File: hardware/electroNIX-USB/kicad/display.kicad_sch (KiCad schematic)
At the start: 69 parts, among them Q10 MMBTA42, Q11 MMBTA92, Q12 MMBTA42, Q13 MMBTA42, Q14 MMBTA42, Q15 MMBTA42, Q16 MMBTA42, Q17 MMBTA42, Q18 MMBTA42, Q19 MMBTA42, Q20 MMBTA42, Q21 MMBTA42, Q22 MMBTA42, Q23 MMBTA42, Q4 MMBTA42, Q5 MMBTA92, Q6 MMBTA42, Q7 MMBTA92, Q8 MMBTA42, Q9 MMBTA92

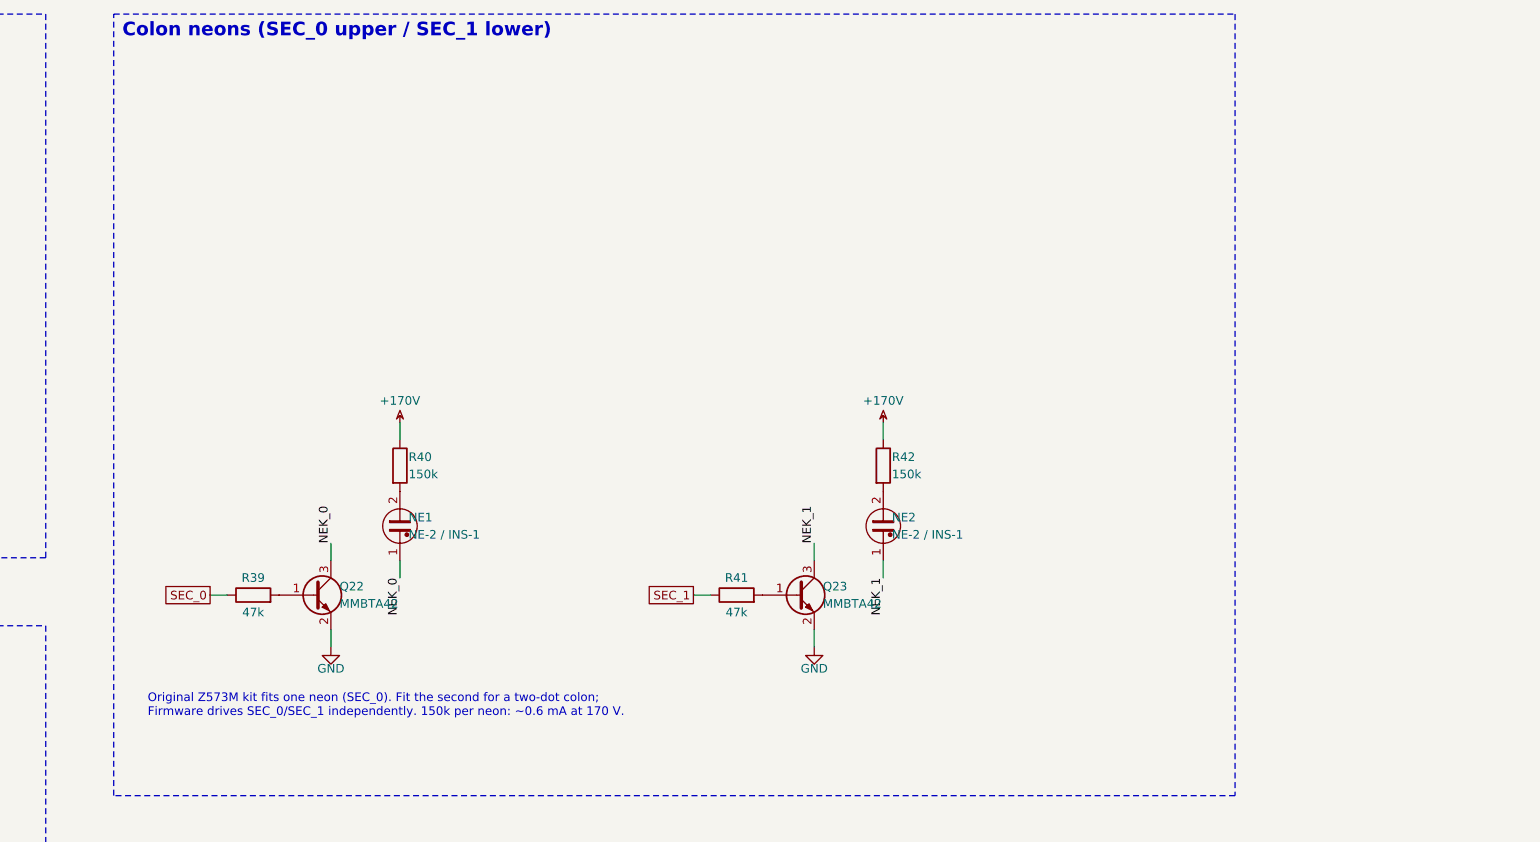
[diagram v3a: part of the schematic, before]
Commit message: electroNIX-USB: socket-adapter footprint, 0.1in neons, 4-tube PCB placement (WIP)
- Z573M socket pins on the electroNIX-2 adapter's 12.6 mm outer ring
  (default footprint), and the direct 9.53 mm footprint resized for the
  1.48 mm socket pins
- Neon_P2.54mm footprint. 6 tubes: HH:MM colon on SEC_0, MM:SS on SEC_1
- SET is a right-angle tact switch; RESET/BOOT use KMR2; low-voltage anode
  resistors moved to 0805
- source/pcb.py: builds the board from the netlist (placement, net
  classes, ESP32 antenna keepout, Freerouting, GND pours, DRC);
  source/fab.sh: fab outputs
- 4-tube board placed (102 x 66 mm, the original kit size), not yet routed

Co-Authored-By: Claude Opus 5.5 <noreply@anthropic.com>
Claude-Session: https://claude.ai/code/session_01AFMfevKEKDGbci8uJGhf4W
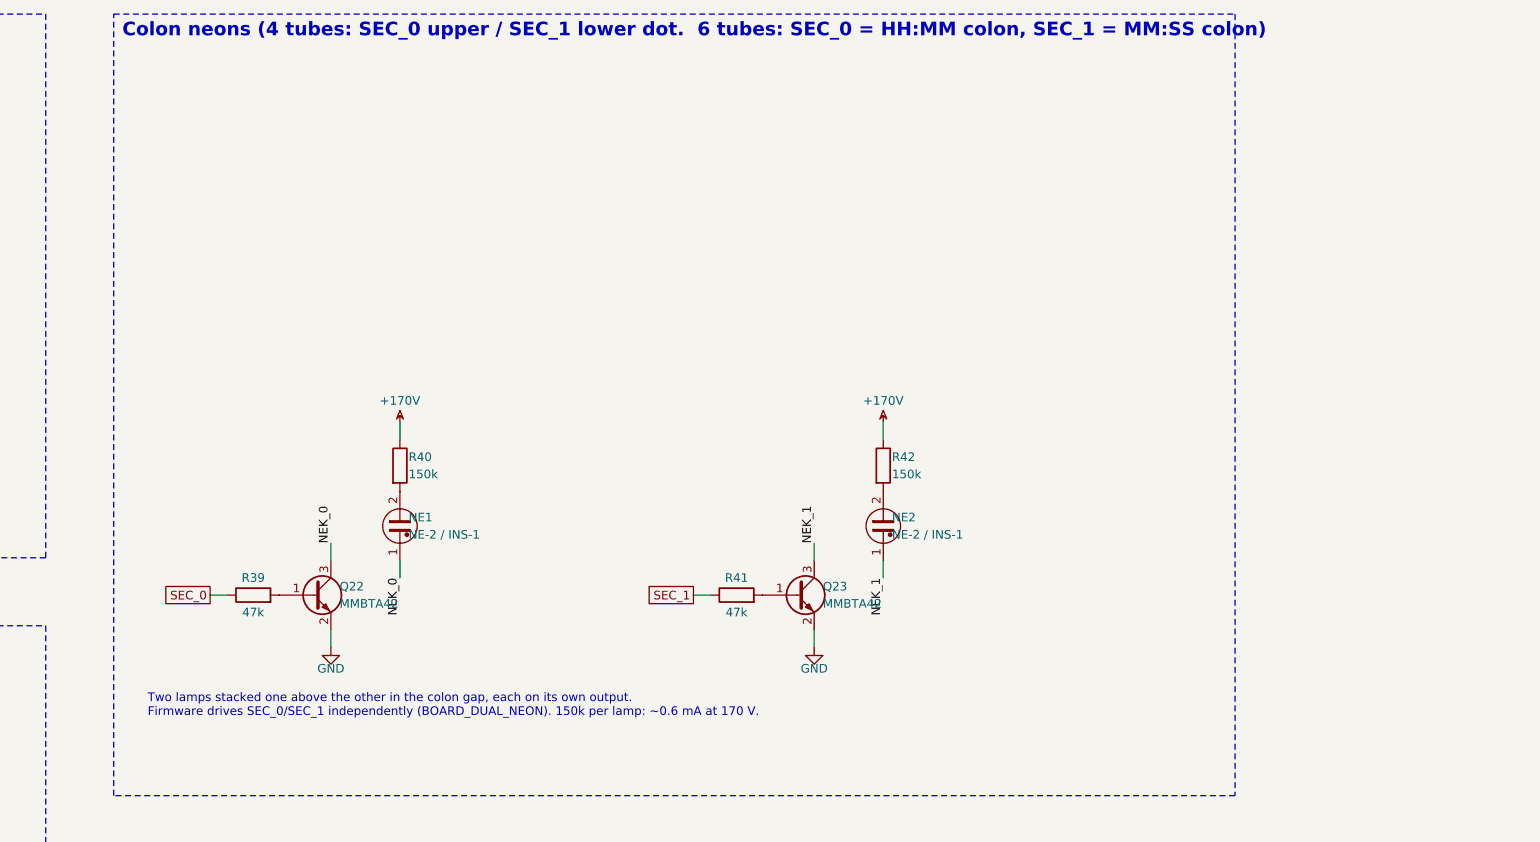
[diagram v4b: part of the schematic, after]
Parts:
- N1, N2, N3, N4: footprint electronix:Nixie_RFT_Z573M -> electronix:Nixie_RFT_Z573M_Adapter
- NE1, NE2: footprint (none) -> electronix:Neon_P2.54mm
- R15, R16, R19, R20, R23, R24, R27, R28: footprint Resistor_SMD:R_1206_3216Metric -> Resistor_SMD:R_0805_2012Metric
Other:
- note added: "Colon neons (4 tubes: SEC_0 upper / SEC_1 lower dot. 6 tubes: SEC_0 = HH:MM colon, SEC_1 = MM:SS colon)"
- note added: "Two lamps stacked one above the other in the colon gap, each on its own output. Firmware drives SEC_0/SEC_1 independently (BOARD_DUAL_NEON). 150k per lamp: ~0.6 mA at 170 V."
- note removed: "Colon neons (SEC_0 upper / SEC_1 lower)"
- note removed: "Original Z573M kit fits one neon (SEC_0). Fit the second for a two-dot colon; Firmware drives SEC_0/SEC_1 independently. 150k per neon: ~0.6 mA at 170 V."
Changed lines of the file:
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@@
       (type none))
 )
-  (text "Colon neons (SEC_0 upper / SEC_1 lower)"
+  (text "Colon neons (4 tubes: SEC_0 upper / SEC_1 lower dot.  6 tubes: SEC_0 = HH:MM colon, SEC_1 = MM:SS colon)"
     (at 411.27 26.27 0)
     (effects
@@
       (justify left top))
 )
-  (text "Original Z573M kit fits one neon (SEC_0). Fit the second for a two-dot colon;\nFirmware drives SEC_0/SEC_1 independently. 150k per neon: ~0.6 mA at 170 V."
+  (text "Two lamps stacked one above the other in the colon gap, each on its own output.\nFirmware drives SEC_0/SEC_1 independently (BOARD_DUAL_NEON). 150k per lamp: ~0.6 mA at 170 V."
     (at 415 125 0)
     (effects
@@
           (size 1.27 1.27))
         (justify left)))
-    (property "Footprint" "Resistor_SMD:R_1206_3216Metric"
+    (property "Footprint" "Resistor_SMD:R_0805_2012Metric"
       (at 52.07 63.5 0)
       (effects
@@
           (size 1.27 1.27))
         (justify left)))
-    (property "Footprint" "Resistor_SMD:R_1206_3216Metric"
+    (property "Footprint" "Resistor_SMD:R_0805_2012Metric"
       (at 59.69 76.2 0)
       (effects
@@
           (size 1.27 1.27))
         (justify left)))
-    (property "Footprint" "Resistor_SMD:R_1206_3216Metric"
+    (property "Footprint" "Resistor_SMD:R_0805_2012Metric"
       (at 142.24 63.5 0)
       (effects
@@
           (size 1.27 1.27))
         (justify left)))
-    (property "Footprint" "Resistor_SMD:R_1206_3216Metric"
+    (property "Footprint" "Resistor_SMD:R_0805_2012Metric"
       (at 149.86 76.2 0)
       (effects
@@
           (size 1.27 1.27))
         (justify left)))
-    (property "Footprint" "Resistor_SMD:R_1206_3216Metric"
+    (property "Footprint" "Resistor_SMD:R_0805_2012Metric"
       (at 232.41 63.5 0)
       (effects
@@
           (size 1.27 1.27))
         (justify left)))
-    (property "Footprint" "Resistor_SMD:R_1206_3216Metric"
+    (property "Footprint" "Resistor_SMD:R_0805_2012Metric"
       (at 240.03 76.2 0)
       (effects
@@
           (size 1.27 1.27))
         (justify left)))
-    (property "Footprint" "Resistor_SMD:R_1206_3216Metric"
+    (property "Footprint" "Resistor_SMD:R_0805_2012Metric"
       (at 322.58 63.5 0)
       (effects
@@
           (size 1.27 1.27))
         (justify left)))
-    (property "Footprint" "Resistor_SMD:R_1206_3216Metric"
+    (property "Footprint" "Resistor_SMD:R_0805_2012Metric"
       (at 330.2 76.2 0)
       (effects
@@
           (size 1.27 1.27))
         (justify left)))
-    (property "Footprint" "electronix:Nixie_RFT_Z573M"
+    (property "Footprint" "electronix:Nixie_RFT_Z573M_Adapter"
       (at 59.69 160.02 0)
       (effects
@@
           (size 1.27 1.27))
         (justify left)))
-    (property "Footprint" "electronix:Nixie_RFT_Z573M"
+    (property "Footprint" "electronix:Nixie_RFT_Z573M_Adapter"
       (at 149.86 160.02 0)
       (effects
@@
           (size 1.27 1.27))
         (justify left)))
-    (property "Footprint" "electronix:Nixie_RFT_Z573M"
+    (property "Footprint" "electronix:Nixie_RFT_Z573M_Adapter"
       (at 240.03 160.02 0)
       (effects
@@
           (size 1.27 1.27))
         (justify left)))
-    (property "Footprint" "electronix:Nixie_RFT_Z573M"
+    (property "Footprint" "electronix:Nixie_RFT_Z573M_Adapter"
       (at 330.2 160.02 0)
       (effects
@@
           (size 1.27 1.27))
         (justify left)))
-    (property "Footprint" ""
+    (property "Footprint" "electronix:Neon_P2.54mm"
       (at 452.12 100.33 0)
       (effects
@@
           (size 1.27 1.27))
         (justify left)))
-    (property "Footprint" ""
+    (property "Footprint" "electronix:Neon_P2.54mm"
       (at 523.24 100.33 0)
       (effects

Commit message: electroNIX-USB: drop all switches, regroup board placement by circuit
- No RESET/BOOT/SET: the firmware reads no button, and the CH340C
  DTR/RTS auto-reset handles flashing. SET's pull-up and cap are gone.
- Boost converter is a compact loop (input caps -> L1 -> FET tab) feeding
  the multiplier columns in chain order.
- ESP32: 3V3 decoupling at pin 2, EN RC at pin 3, HV feedback divider and
  clamp at IO35; auto-reset between the CH340C and the module's UART pins.
- Front band spread out: output cap + KBIAS left, cathode row, one anode
  cluster under each tube.
- 6-tube board placed too (150 x 66 mm). Both boards unrouted.

Co-Authored-By: Claude Opus 5.5 <noreply@anthropic.com>
Claude-Session: https://claude.ai/code/session_01AFMfevKEKDGbci8uJGhf4W
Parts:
- removed C22: 2u2 50V, Capacitor_SMD:C_1206_3216Metric, symbol Device:C
- removed R44: 100k, Resistor_SMD:R_0805_2012Metric, symbol Device:R
- added C21: 2u2 50V, Capacitor_SMD:C_1206_3216Metric, symbol Device:C
- added R12: 15k, Resistor_SMD:R_0805_2012Metric, symbol Device:R
- R13, R17, R21, R25: value 15k -> 430k; footprint Resistor_SMD:R_0805_2012Metric -> Resistor_SMD:R_1206_3216Metric
- R14, R18, R22, R26, R43: value 430k -> 100k; footprint Resistor_SMD:R_1206_3216Metric -> Resistor_SMD:R_0805_2012Metric
- R15, R19, R23, R27: value 100k -> 5k6
- R16, R20, R24: value 5k6 -> 15k
- R28: value 5k6 -> 6k8
- R38: value 6k8 -> 47k
- R39, R41: value 47k -> 150k; footprint Resistor_SMD:R_0805_2012Metric -> Resistor_SMD:R_1206_3216Metric
- R40: value 150k -> 47k; footprint Resistor_SMD:R_1206_3216Metric -> Resistor_SMD:R_0805_2012Metric
- R42: value 150k -> 430k
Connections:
- net +170V: now also R14.1, R18.1, R22.1, R26.1, R39.1, R41.1; no longer R15.1, R19.1, R23.1, R27.1, R40.1, R43.1
- net A_1: now also R15.2; no longer R16.2
- net A_2: now also R19.2; no longer R20.2
- net A_3: now also R23.2; no longer R24.2
- net A_4: now also R27.2; no longer R28.2
- net C_0: now also R28.1; no longer R29.1
- net C_1: now also R29.1; no longer R30.1
- net C_2: now also R30.1; no longer R31.1
- net C_3: now also R31.1; no longer R32.1
- net C_4: now also R32.1; no longer R33.1
- net C_5: now also R33.1; no longer R34.1
- net C_6: now also R34.1; no longer R35.1
- net C_7: now also R35.1; no longer R36.1
- net C_8: now also R36.1; no longer R37.1
- net C_9: now also R37.1; no longer R38.1
- net GND: now also R43.2, C21.2
- net KBIAS: now also R42.2, R43.1, C21.1; no longer R43.2
- net SEC_0: now also R38.1; no longer R39.1
- net SEC_1: now also R40.1; no longer R41.1
- net W_1: now also R12.1; no longer R13.1
- net W_2: now also R16.1; no longer R17.1
- net W_3: now also R20.1; no longer R21.1
- net W_4: now also R24.1; no longer R25.1
- net at Q6.1 (B): now also R16.2; no longer R17.2
- net at Q6.3 (C): now also R17.2; no longer R18.2
- net at Q7.3 (C): now also R19.1; no longer R20.1
- net at Q9.3 (C): now also R23.1; no longer R24.1
- net at Q11.3 (C): now also R27.1; no longer R28.1
- net at Q5.3 (C): now also R15.1; no longer R16.1
- net at Q20.1 (B): now also R36.2; no longer R37.2
- net at R34.2: now also Q18.1 (B); no longer Q17.1 (B)
- net at Q14.1 (B): now also R30.2; no longer R31.2
- net at Q19.1 (B): now also R35.2; no longer R36.2
- net at Q12.1 (B): now also R28.2; no longer R29.2
- net at R40.2: now also Q23.1 (B); no longer NE1.2
- net at Q13.1 (B): now also R29.2; no longer R30.2
- net at R41.2: now also NE2.2; no longer Q23.1 (B)
- net at Q4.1 (B): now also R12.2; no longer R13.2
- net at R14.2: now also Q5.1 (B), R13.1; no longer Q4.3 (C)
- net at Q8.1 (B): now also R20.2; no longer R21.2
- net at Q8.3 (C): now also R21.2; no longer R22.2
- net at Q10.1 (B): now also R24.2; no longer R25.2
- net at R26.2: now also Q11.1 (B), R25.1; no longer Q10.3 (C)
- net at R33.2: now also Q17.1 (B); no longer Q16.1 (B)
- net at R32.2: now also Q16.1 (B); no longer Q15.1 (B)
- net at Q21.1 (B): now also R37.2; no longer R38.2
- net at Q22.1 (B): now also R38.2; no longer R39.2
- new net: Q7.1 (B), R17.1, R18.2
- new net: Q4.3 (C), R13.2
- new net: Q10.3 (C), R25.2
- new net: Q9.1 (B), R21.1, R22.2
- new net: NE1.2, R39.2
- new net: Q15.1 (B), R31.2
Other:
- moved on the sheet: R13, R14, R15, R16, R17, R18, R19, R20, R21, R22, R23, R24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
